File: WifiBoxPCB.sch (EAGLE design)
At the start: 3 parts, among them J1 1140084168, U1 MCP73871-2CCI/ML, U2 AZ1117EH-5.0TRG1

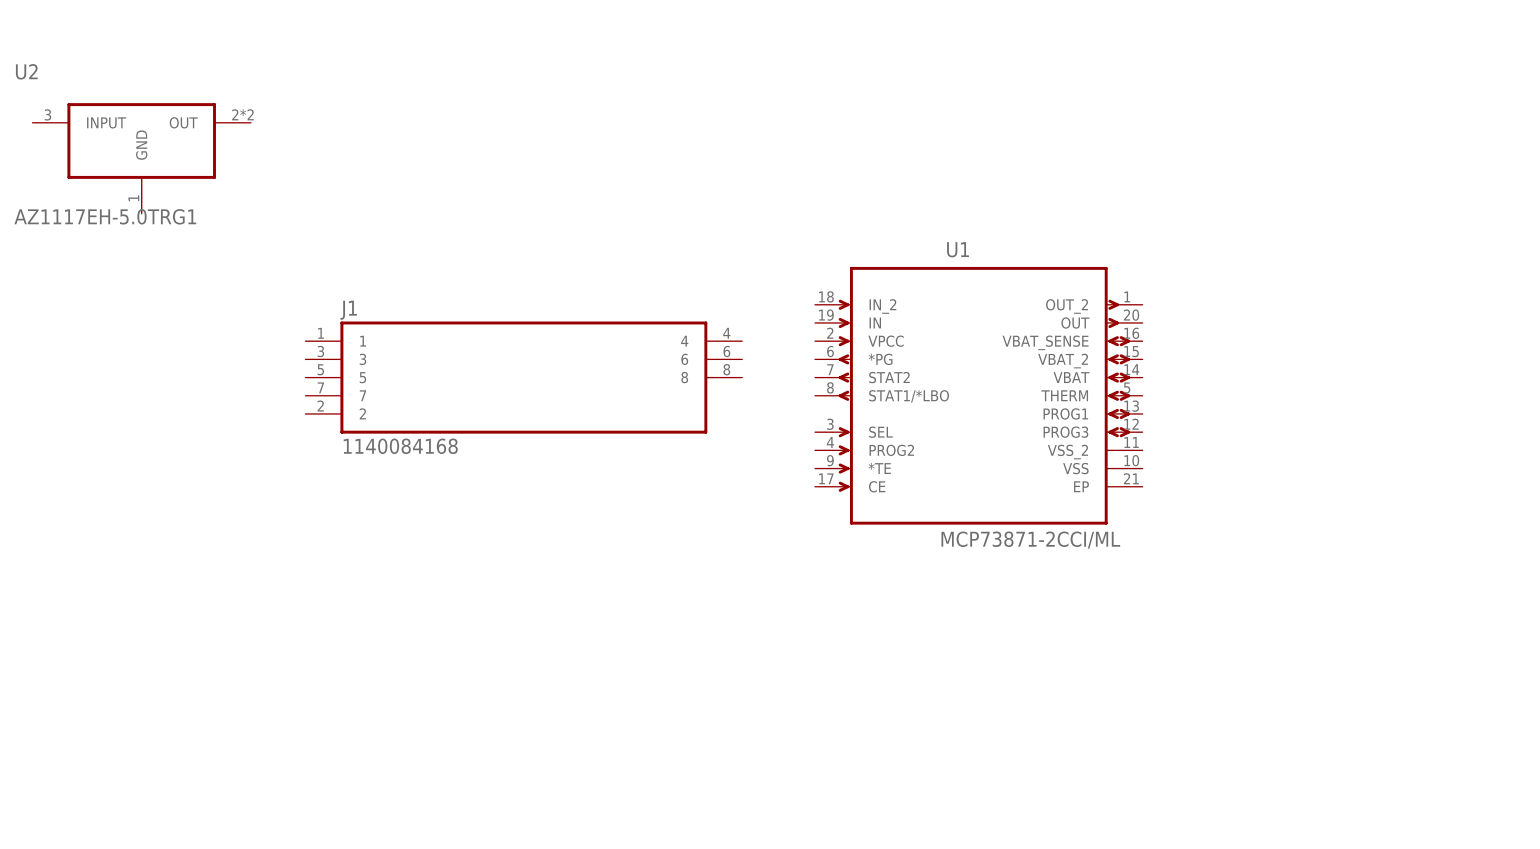
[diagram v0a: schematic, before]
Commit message: reset board and schematic down to just the micro SD
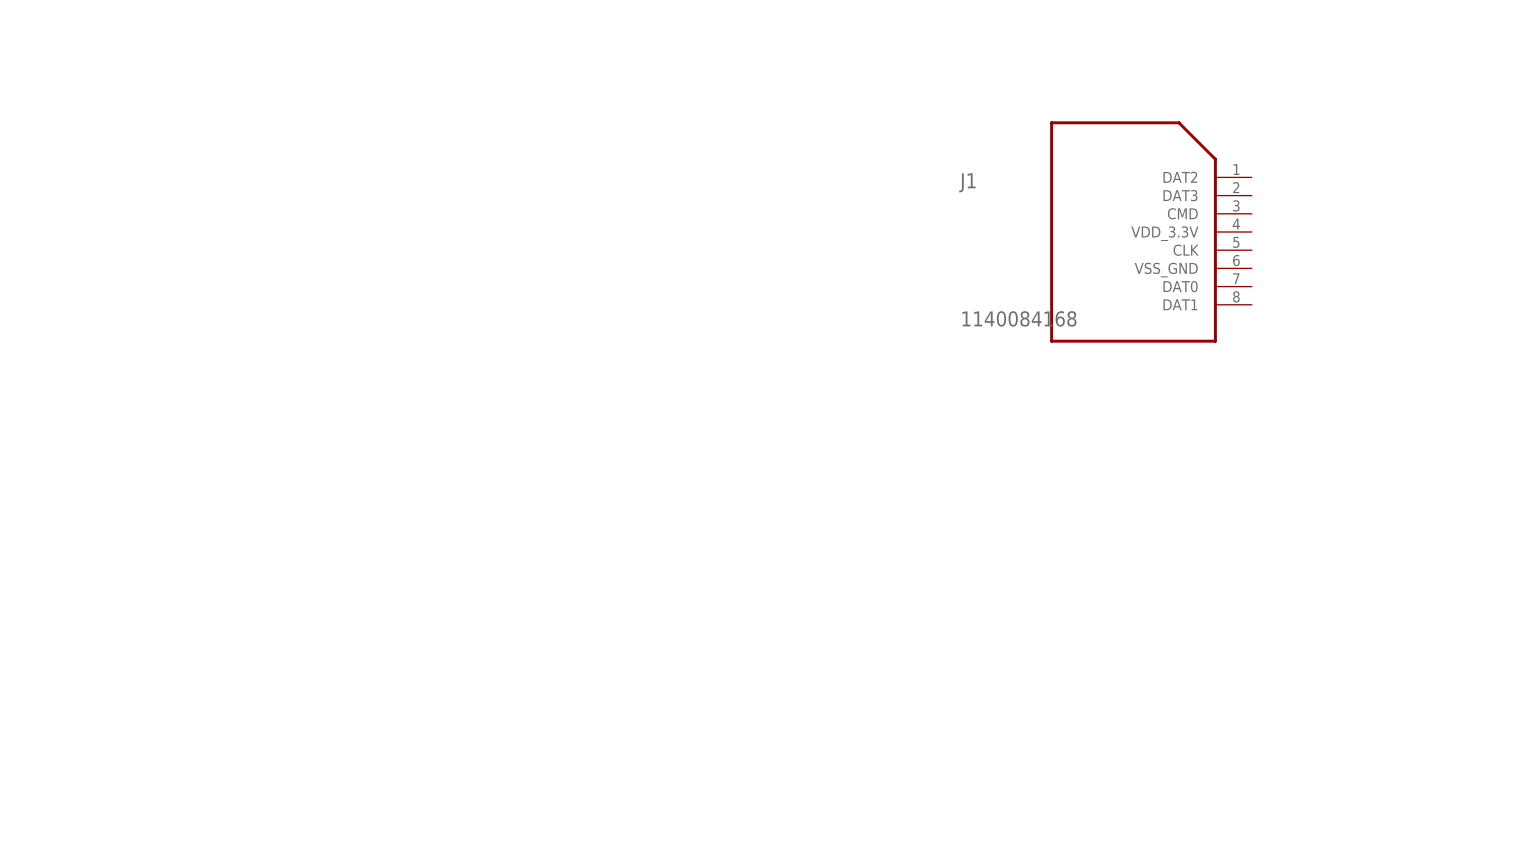
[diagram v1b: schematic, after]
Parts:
- removed U1: MCP73871-2CCI/ML, MCP73871-2CCI_ML:MCP73871-2CCI/ML
- removed U2: AZ1117EH-5.0TRG1, AZ1117EH-5.0TRG1:AZ1117EH-5.0TRG1
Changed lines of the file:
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@@
 <part name="FRAME1" library="frames" library_urn="urn:adsk.eagle:library:229" deviceset="LETTER_L" device=""/>
 <part name="J1" library="1140084168" deviceset="1140084168" device=""/>
-<part name="U1" library="MCP73871-2CCI_ML" deviceset="MCP73871-2CCI/ML" device=""/>
-<part name="U2" library="AZ1117EH-5.0TRG1" deviceset="AZ1117EH-5.0TRG1" device=""/>
 </parts>
 <sheets>
@@
 <attribute name="DRAWING_NAME" x="165.1" y="19.05" size="2.54" layer="94"/>
 </instance>
-<instance part="J1" gate="G$1" x="99.06" y="109.22" smashed="yes">
-<attribute name="NAME" x="73.5914" y="117.86326875" size="2.08841875" layer="95" ratio="10" rot="SR0"/>
-<attribute name="VALUE" x="73.6307" y="98.5877" size="2.085209375" layer="96" ratio="10" rot="SR0"/>
-</instance>
-<instance part="U1" gate="A" x="162.56" y="109.22" smashed="yes">
-<attribute name="NAME" x="157.903590625" y="126.039" size="2.08648125" layer="95" ratio="10" rot="SR0"/>
-<attribute name="VALUE" x="157.09061875" y="85.6126" size="2.086" layer="96" ratio="10" rot="SR0"/>
-</instance>
-<instance part="U2" gate="G$1" x="45.72" y="142.24" smashed="yes">
-<attribute name="NAME" x="27.94" y="150.86" size="2.0828" layer="95" ratio="10" rot="SR0"/>
-<attribute name="VALUE" x="27.94" y="130.62" size="2.0828" layer="96" ratio="10" rot="SR0"/>
+<instance part="J1" gate="G$1" x="185.42" y="127" smashed="yes">
+<attribute name="NAME" x="159.9514" y="135.64326875" size="2.08841875" layer="95" ratio="10" rot="SR0"/>
+<attribute name="VALUE" x="159.9907" y="116.3677" size="2.085209375" layer="96" ratio="10" rot="SR0"/>
 </instance>
 </instances>

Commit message: Add frame, +5V, +3.3V, GND, 2x20 connector customized for Raspberry Pi, customized MicroSD devices to library, change Schematic to use parts from ConnectBox Library, start to wire MicroSD socket to Pi 40 pin connector.
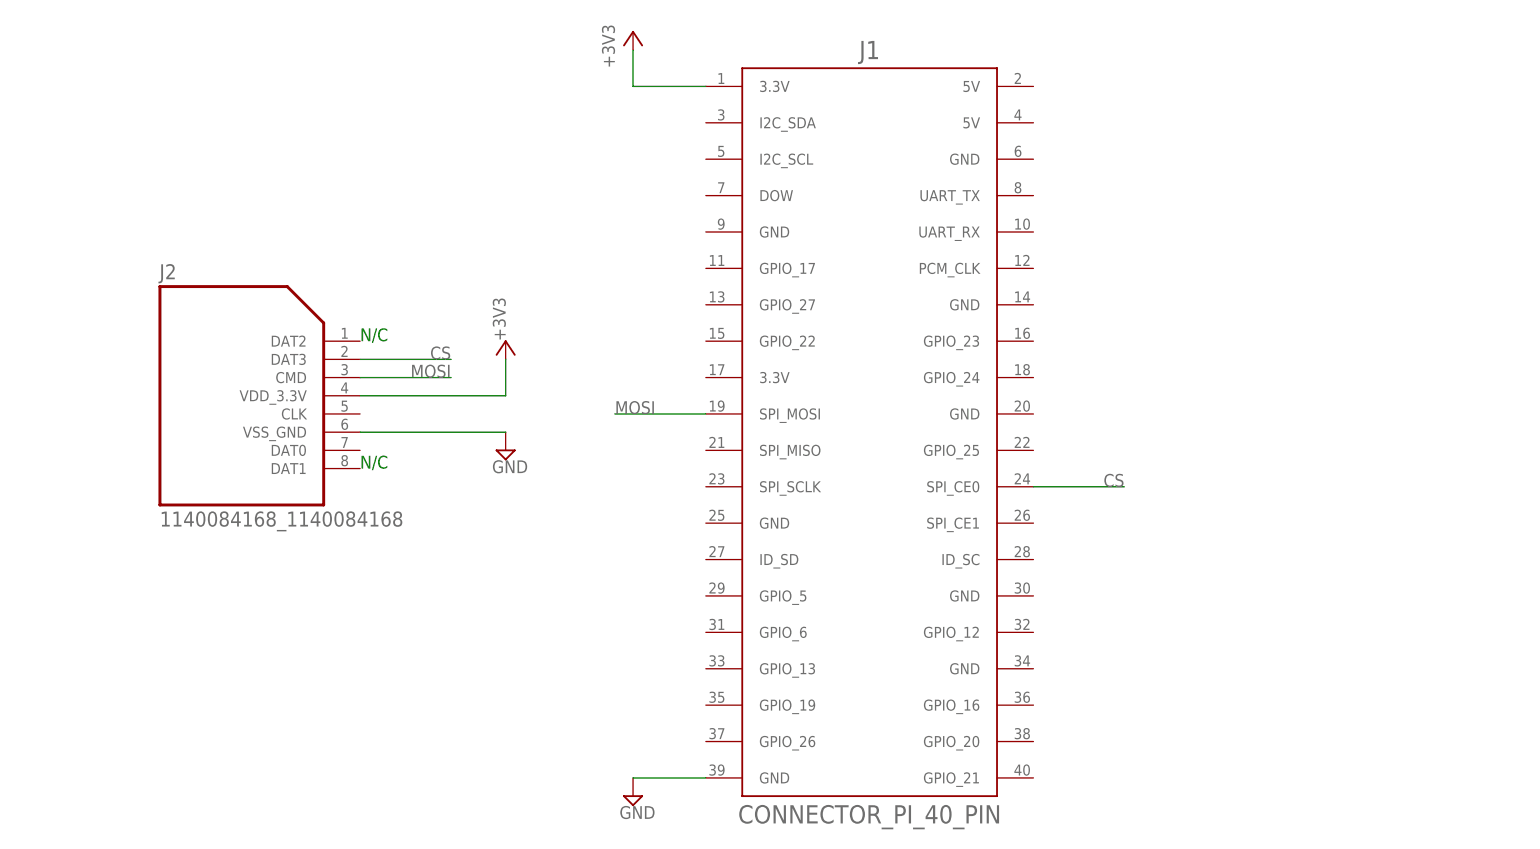
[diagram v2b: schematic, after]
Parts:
- added J2: 1140084168_1140084168, ConnectBox_2019:1140084168_1140084168
- J1: value 1140084168 -> CONNECTOR_PI_40_PIN; device 1140084168:1140084168 -> ConnectBox_2019:CONNECTOR_PI_40_PIN
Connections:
- new net +3V3: J1.3.3V@1, J2.VDD_3.3V@4
- new net CS: J1.SPI_CE0@24, J2.DAT3@2
- new net GND: J1.GND@39, J2.VSS_GND@6
- new net MOSI: J1.SPI_MOSI@19, J2.CMD@3
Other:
- note added: "N/C"

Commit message: PCB routed contains microSD and OLED screen
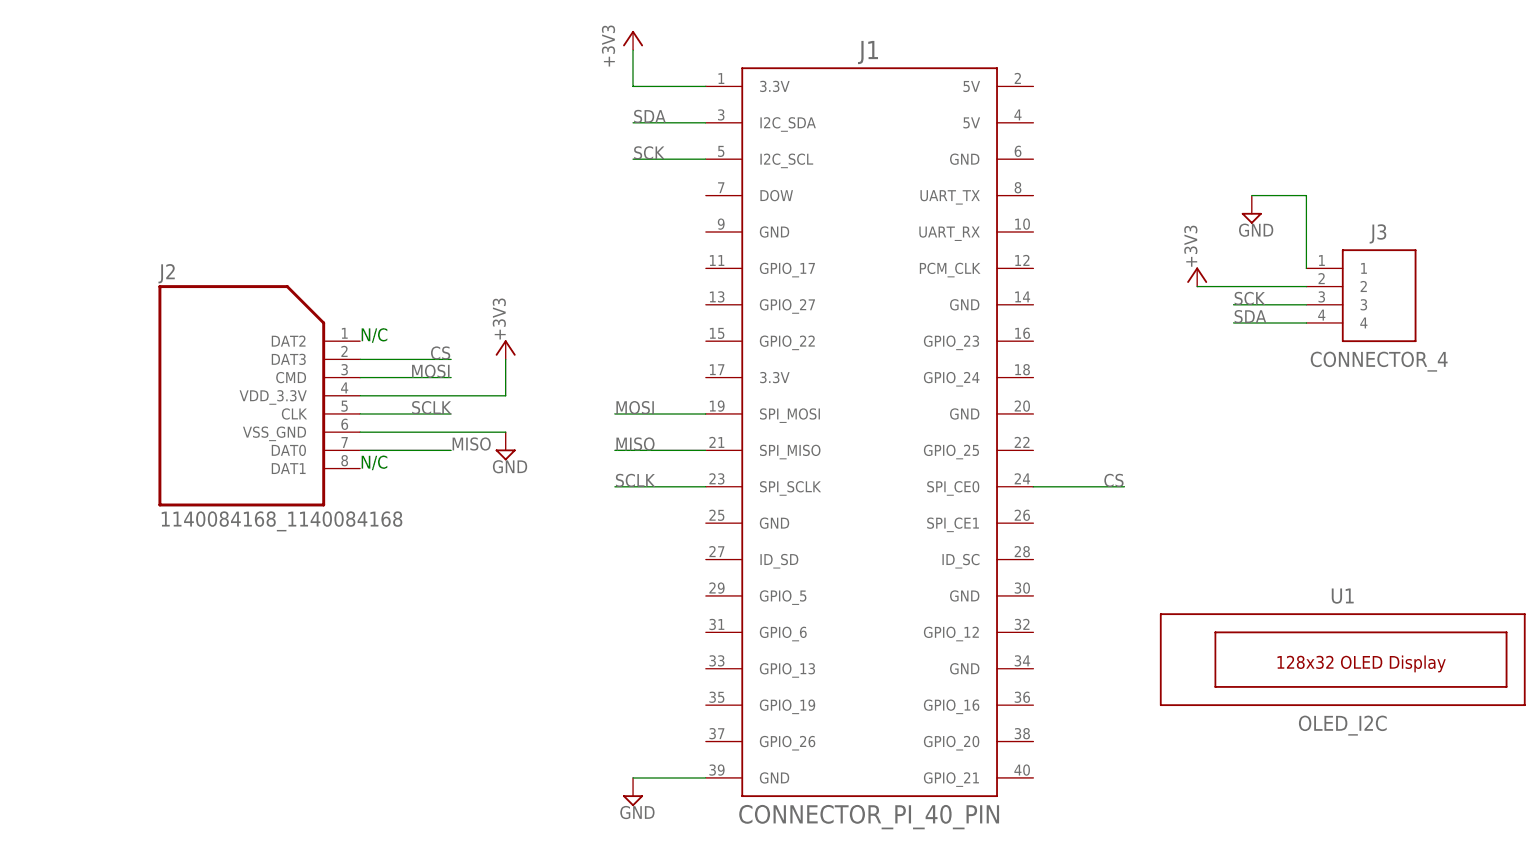
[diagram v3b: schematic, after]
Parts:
- added J3: CONNECTOR_4, ConnectBox_2019:CONNECTOR_4
- added U1: OLED_I2C, ConnectBox_2019:OLED_I2C
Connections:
- new net MISO: J1.SPI_MISO@21, J2.DAT0@7
- new net SCK: J1.I2C_SCL@5, J3.3
- new net SCLK: J1.SPI_SCLK@23, J2.CLK@5
- new net SDA: J1.I2C_SDA@3, J3.4
- net +3V3: now also J3.2
- net GND: now also J3.1
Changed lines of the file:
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@@
 <?xml version="1.0" encoding="utf-8"?>
 <!DOCTYPE eagle SYSTEM "eagle.dtd">
-<eagle version="9.3.1">
+<eagle version="9.2.2">
 <drawing>
 <settings>
@@
 <setting verticaltext="up"/>
 </settings>
-<grid distance="0.1" unitdist="inch" unit="inch" style="lines" multiple="1" display="yes" altdistance="0.01" altunitdist="inch" altunit="inch"/>
+<grid distance="0.1" unitdist="inch" unit="inch" style="lines" multiple="1" display="no" altdistance="0.01" altunitdist="inch" altunit="inch"/>
 <layers>
 <layer number="1" name="Top" color="4" fill="1" visible="no" active="no"/>
@@
 <layer number="56" name="wert" color="7" fill="1" visible="no" active="no"/>
 <layer number="57" name="tCAD" color="7" fill="1" visible="no" active="no"/>
+<layer number="58" name="bCad" color="7" fill="1" visible="no" active="no"/>
 <layer number="59" name="tCarbon" color="7" fill="1" visible="no" active="no"/>
 <layer number="60" name="bCarbon" color="7" fill="1" visible="no" active="no"/>
@@
 <part name="SUPPLY1" library="ConnectBox_2019" deviceset="GND" device=""/>
 <part name="SUPPLY2" library="ConnectBox_2019" deviceset="GND" device=""/>
+<part name="U1" library="ConnectBox_2019" deviceset="OLED_I2C" device=""/>
+<part name="+3V3" library="ConnectBox_2019" deviceset="+3V3" device=""/>
+<part name="SUPPLY3" library="ConnectBox_2019" deviceset="GND" device=""/>
+<part name="J3" library="ConnectBox_2019" deviceset="CONNECTOR_4" device=""/>
 </parts>
 <sheets>
@@
 <attribute name="VALUE" x="112.395" y="47.625" size="1.778" layer="96"/>
 </instance>
+<instance part="U1" gate="G$1" x="213.36" y="71.12" smashed="yes">
+<attribute name="VALUE" x="213.36" y="60.96" size="2.0828" layer="96" rot="R180" align="center"/>
+<attribute name="NAME" x="213.36" y="78.74" size="2.0828" layer="95" rot="R180" align="center"/>
+</instance>
+<instance part="+3V3" gate="G$1" x="193.04" y="124.46" smashed="yes">
+<attribute name="VALUE" x="193.04" y="124.46" size="1.778" layer="96" rot="R90"/>
+</instance>
+<instance part="SUPPLY3" gate="GND" x="200.66" y="132.08" smashed="yes">
+<attribute name="VALUE" x="198.755" y="128.905" size="1.778" layer="96"/>
+</instance>
+<instance part="J3" gate="G$1" x="218.44" y="121.92" smashed="yes" rot="MR0">
+<attribute name="VALUE" x="218.44" y="111.76" size="2.0828" layer="96" rot="MR180" align="center"/>
+<attribute name="NAME" x="218.44" y="129.54" size="2.0828" layer="95" rot="MR180" align="center"/>
+</instance>
 </instances>
 <busses>
@@
 <wire x1="96.52" y1="106.68" x2="76.2" y2="106.68" width="0.1524" layer="91"/>
 </segment>
+<segment>
+<pinref part="+3V3" gate="G$1" pin="+3V3"/>
+<wire x1="193.04" y1="121.92" x2="208.28" y2="121.92" width="0.1524" layer="91"/>
+<pinref part="J3" gate="G$1" pin="2"/>
+</segment>
 </net>
 <net name="GND" class="0">
@@
 <wire x1="114.3" y1="53.34" x2="124.46" y2="53.34" width="0.1524" layer="91"/>
 </segment>
+<segment>
+<pinref part="SUPPLY3" gate="GND" pin="GND"/>
+<wire x1="200.66" y1="134.62" x2="208.28" y2="134.62" width="0.1524" layer="91"/>
+<wire x1="208.28" y1="134.62" x2="208.28" y2="124.46" width="0.1524" layer="91"/>
+<pinref part="J3" gate="G$1" pin="1"/>
+</segment>
+</net>
+<net name="SCLK" class="0">
+<segment>
+<pinref part="J2" gate="G$1" pin="CLK@5"/>
+<wire x1="88.9" y1="104.14" x2="76.2" y2="104.14" width="0.1524" layer="91"/>
+<label x="88.9" y="104.14" size="1.778" layer="95" rot="MR0"/>
+</segment>
+<segment>
+<pinref part="J1" gate="G$1" pin="SPI_SCLK@23"/>
+<wire x1="111.76" y1="93.98" x2="124.46" y2="93.98" width="0.1524" layer="91"/>
+<label x="111.76" y="93.98" size="1.778" layer="95"/>
+</segment>
+</net>
+<net name="MISO" class="0">
+<segment>
+<pinref part="J2" gate="G$1" pin="DAT0@7"/>
+<wire x1="88.9" y1="99.06" x2="76.2" y2="99.06" width="0.1524" layer="91"/>
+<label x="88.9" y="99.06" size="1.778" layer="95"/>
+</segment>
+<segment>
+<pinref part="J1" gate="G$1" pin="SPI_MISO@21"/>
+<wire x1="111.76" y1="99.06" x2="124.46" y2="99.06" width="0.1524" layer="91"/>
+<label x="111.76" y="99.06" size="1.778" layer="95"/>
+</segment>
+</net>
+<net name="SCK" class="0">
+<segment>
+<wire x1="208.28" y1="119.38" x2="198.12" y2="119.38" width="0.1524" layer="91"/>
+<label x="198.12" y="119.38" size="1.778" layer="95"/>
+<pinref part="J3" gate="G$1" pin="3"/>
+</segment>
+<segment>
+<pinref part="J1" gate="G$1" pin="I2C_SCL@5"/>
+<wire x1="124.46" y1="139.7" x2="114.3" y2="139.7" width="0.1524" layer="91"/>
+<label x="114.3" y="139.7" size="1.778" layer="95"/>
+</segment>
+</net>
+<net name="SDA" class="0">
+<segment>
+<wire x1="208.28" y1="116.84" x2="198.12" y2="116.84" width="0.1524" layer="91"/>
+<label x="198.12" y="116.84" size="1.778" layer="95"/>
+<pinref part="J3" gate="G$1" pin="4"/>
+</segment>
+<segment>
+<pinref part="J1" gate="G$1" pin="I2C_SDA@3"/>
+<wire x1="114.3" y1="144.78" x2="124.46" y2="144.78" width="0.1524" layer="91"/>
+<label x="114.3" y="144.78" size="1.778" layer="95"/>
+</segment>
 </net>
 </nets>
 </sheet>
 </sheets>
+<errors>
+</errors>
 </schematic>
 </drawing>

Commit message: update microsd, OLED schematic "value"s.
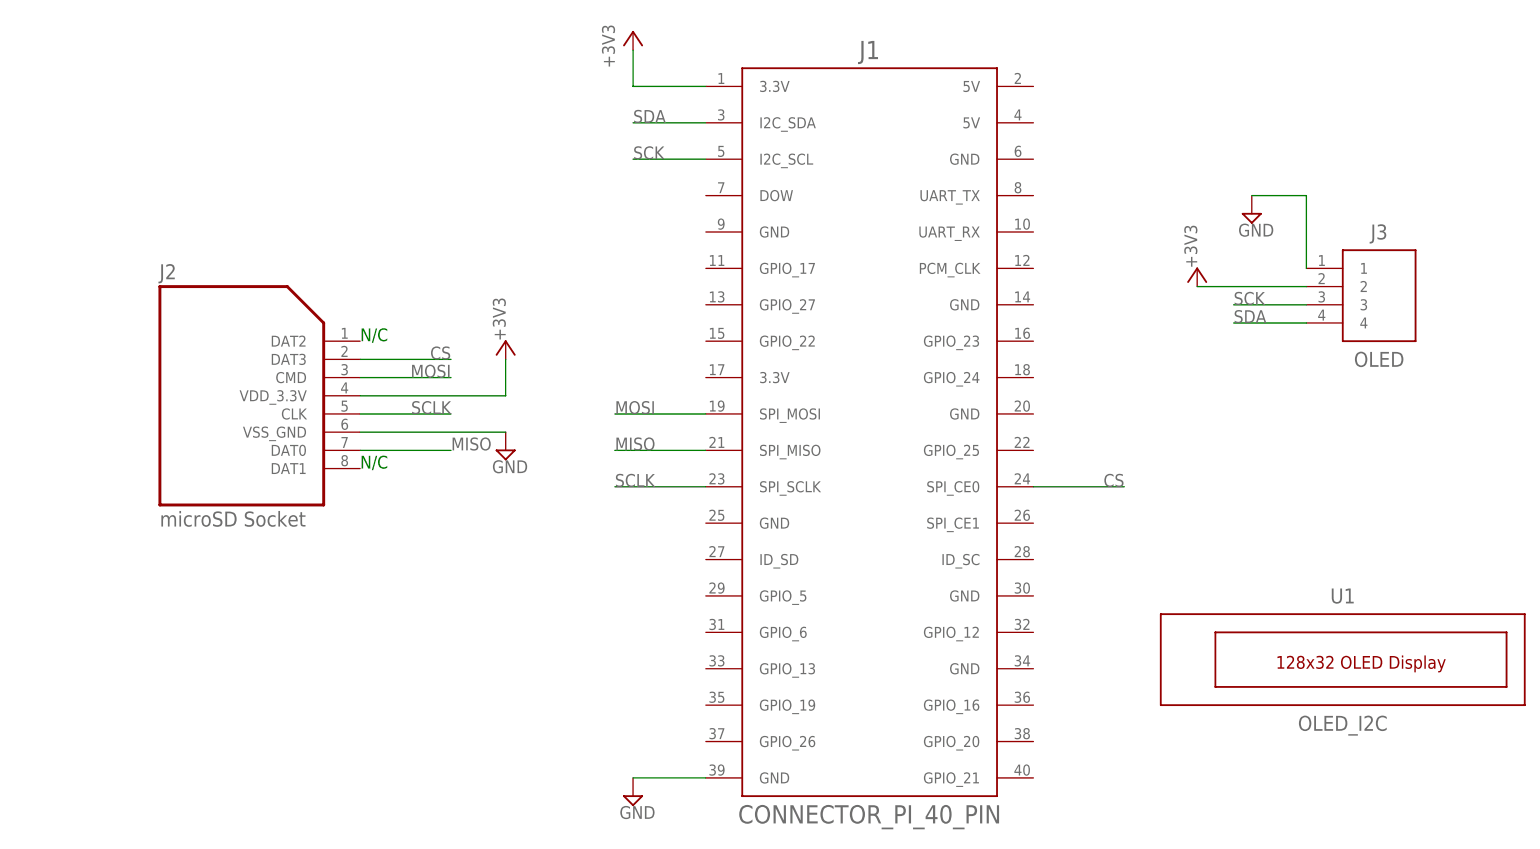
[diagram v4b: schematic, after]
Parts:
- J2: value 1140084168_1140084168 -> microSD Socket
- J3: value CONNECTOR_4 -> OLED
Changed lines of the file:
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@@
 <?xml version="1.0" encoding="utf-8"?>
 <!DOCTYPE eagle SYSTEM "eagle.dtd">
-<eagle version="9.2.2">
+<eagle version="9.3.1">
 <drawing>
 <settings>
@@
 <parts>
 <part name="FRAME1" library="ConnectBox_2019" deviceset="FRAMES_LETTER_L" device=""/>
-<part name="J2" library="ConnectBox_2019" deviceset="1140084168_1140084168" device=""/>
+<part name="J2" library="ConnectBox_2019" deviceset="1140084168_1140084168" device="" value="microSD Socket"/>
 <part name="J1" library="ConnectBox_2019" deviceset="CONNECTOR_PI_40_PIN" device=""/>
 <part name="+3V1" library="ConnectBox_2019" deviceset="+3V3" device=""/>
@@
 <part name="+3V3" library="ConnectBox_2019" deviceset="+3V3" device=""/>
 <part name="SUPPLY3" library="ConnectBox_2019" deviceset="GND" device=""/>
-<part name="J3" library="ConnectBox_2019" deviceset="CONNECTOR_4" device=""/>
+<part name="J3" library="ConnectBox_2019" deviceset="CONNECTOR_4" device="" value="OLED"/>
 </parts>
 <sheets>
